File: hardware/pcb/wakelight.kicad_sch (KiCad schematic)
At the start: 35 parts, among them J1 USB-C 16P, J2 DMX OUT, Q1 SS8050, Q2 SS8050, SW1 EN, SW2 BOOT, U1 ESP32-WROOM-32E-N8, U2 CH340C, U3 AMS1117-3.3, U4 THVD1410DR

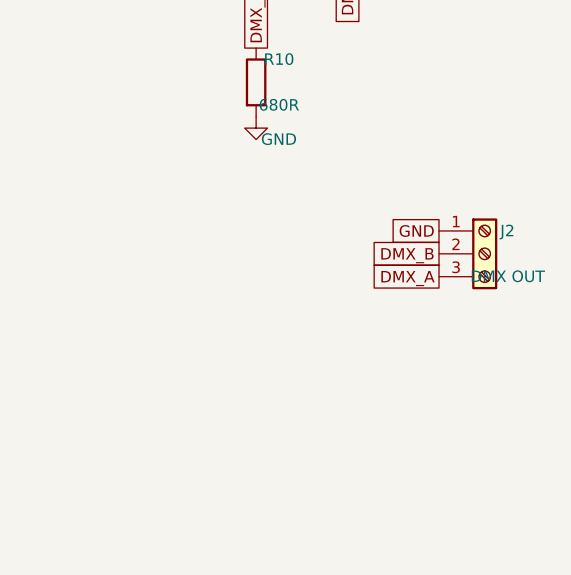
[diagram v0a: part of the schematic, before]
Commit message: WakeLight v1.1: PCB-mount Neutrik NC5FAH 5-pin XLR DMX output
Board widened to 66x42mm, XLR footprint verified against the official
Neutrik drilling plan, regulator corner re-placed, DRC clean (0 errors,
0 unconnected). Schematic updated (ERC clean), v1.0 terminal-variant fab
files archived, docs and sourcing updated.

Co-Authored-By: Claude Fable 5 <noreply@anthropic.com>
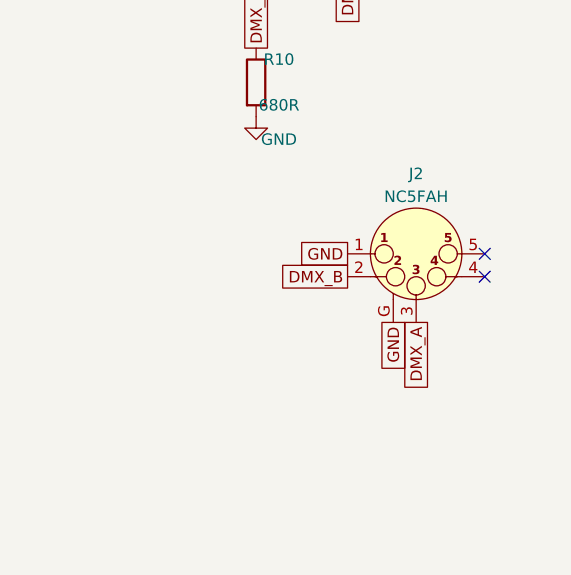
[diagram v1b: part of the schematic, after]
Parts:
- J2: value DMX OUT -> NC5FAH; footprint TerminalBlock_Phoenix:TerminalBlock_Phoenix_MKDS-1,5-3-5.08_1x03_P5.08mm_Horizontal -> Connector_Audio:Jack_XLR_Neutrik_NC5FAH_Horizontal; symbol Connector:Screw_Terminal_01x03 -> Connector_Audio:XLR5_Ground
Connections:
- net GND: now also J2.G
- no-connect marks 27 -> 29
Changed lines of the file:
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@@
 		(title "WakeLight Controller")
 		(date "2026-06-10")
-		(rev "1.0")
+		(rev "1.1")
 		(company "Amodo Design")
 		(comment 1 "USB-C / CH340C / ESP32-WROOM-32E / THVD1410 RS-485 DMX")
@@
 	(global_label "IO0" (shape passive) (at 195.58 116.84 180) (effects (font (size 1.27 1.27)) (justify right)) (property "Intersheetrefs" "${INTERSHEET_REFS}" (at 195.58 116.84 0) (effects (font (size 1.27 1.27)) (hide yes))))
 	(global_label "GND" (shape passive) (at 205.74 116.84 0) (effects (font (size 1.27 1.27)) (justify left)) (property "Intersheetrefs" "${INTERSHEET_REFS}" (at 205.74 116.84 0) (effects (font (size 1.27 1.27)) (hide yes))))
-	(symbol (lib_id "Connector:Screw_Terminal_01x03") (at 401.32 148.59 0) (unit 1)
-	 (exclude_from_sim no) (in_bom yes) (on_board yes) (dnp no)
-	 (property "Reference" "J2" (at 403.86 146.05 0) (effects (font (size 1.27 1.27))))
-	 (property "Value" "DMX OUT" (at 403.86 151.13 0) (effects (font (size 1.27 1.27))))
-	 (property "Footprint" "TerminalBlock_Phoenix:TerminalBlock_Phoenix_MKDS-1,5-3-5.08_1x03_P5.08mm_Horizontal" (at 401.32 148.59 0) (effects (font (size 1.27 1.27)) (hide yes)))
-	 (property "Datasheet" "" (at 401.32 148.59 0) (effects (font (size 1.27 1.27)) (hide yes)))
+	(symbol (lib_id "Connector_Audio:XLR5_Ground") (at 393.7 148.59 0) (unit 1)
+	 (exclude_from_sim no) (in_bom yes) (on_board yes) (dnp no)
+	 (property "Reference" "J2" (at 393.7 139.7 0) (effects (font (size 1.27 1.27))))
+	 (property "Value" "NC5FAH" (at 393.7 142.24 0) (effects (font (size 1.27 1.27))))
+	 (property "Footprint" "Connector_Audio:Jack_XLR_Neutrik_NC5FAH_Horizontal" (at 393.7 148.59 0) (effects (font (size 1.27 1.27)) (hide yes)))
+	 (property "Datasheet" "" (at 393.7 148.59 0) (effects (font (size 1.27 1.27)) (hide yes)))
 	 (pin "1")
 	 (pin "2")
 	 (pin "3")
+	 (pin "4")
+	 (pin "5")
+	 (pin "G")
 	 (instances (project "wakelight" (path "/a2643ac4-cbbd-530c-93c4-588f70f6c903" (reference "J2") (unit 1))))
 	)
-	(global_label "GND" (shape passive) (at 396.24 146.05 180) (effects (font (size 1.27 1.27)) (justify right)) (property "Intersheetrefs" "${INTERSHEET_REFS}" (at 396.24 146.05 0) (effects (font (size 1.27 1.27)) (hide yes))))
-	(global_label "DMX_B" (shape passive) (at 396.24 148.59 180) (effects (font (size 1.27 1.27)) (justify right)) (property "Intersheetrefs" "${INTERSHEET_REFS}" (at 396.24 148.59 0) (effects (font (size 1.27 1.27)) (hide yes))))
-	(global_label "DMX_A" (shape passive) (at 396.24 151.13 180) (effects (font (size 1.27 1.27)) (justify right)) (property "Intersheetrefs" "${INTERSHEET_REFS}" (at 396.24 151.13 0) (effects (font (size 1.27 1.27)) (hide yes))))
+	(global_label "GND" (shape passive) (at 386.08 148.59 180) (effects (font (size 1.27 1.27)) (justify right)) (property "Intersheetrefs" "${INTERSHEET_REFS}" (at 386.08 148.59 0) (effects (font (size 1.27 1.27)) (hide yes))))
+	(global_label "DMX_B" (shape passive) (at 386.08 151.13 180) (effects (font (size 1.27 1.27)) (justify right)) (property "Intersheetrefs" "${INTERSHEET_REFS}" (at 386.08 151.13 0) (effects (font (size 1.27 1.27)) (hide yes))))
+	(global_label "DMX_A" (shape passive) (at 393.7 156.21 270) (effects (font (size 1.27 1.27)) (justify right)) (property "Intersheetrefs" "${INTERSHEET_REFS}" (at 393.7 156.21 0) (effects (font (size 1.27 1.27)) (hide yes))))
+	(global_label "GND" (shape passive) (at 391.16 156.21 270) (effects (font (size 1.27 1.27)) (justify right)) (property "Intersheetrefs" "${INTERSHEET_REFS}" (at 391.16 156.21 0) (effects (font (size 1.27 1.27)) (hide yes))))
+	(no_connect (at 401.32 151.13))
+	(no_connect (at 401.32 148.59))
 	(symbol (lib_id "Mechanical:MountingHole") (at 30.48 236.22 0) (unit 1)
 	 (exclude_from_sim no) (in_bom yes) (on_board yes) (dnp no)
